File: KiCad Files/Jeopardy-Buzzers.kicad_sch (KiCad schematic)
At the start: 13 parts, among them J1 USB_C_Receptacle, U1 CH32V003FxUx, U2 CH340N, U3 NRF24L01_Breakout, U4 TPD2EUSB30, U5 AMS1117-3.3

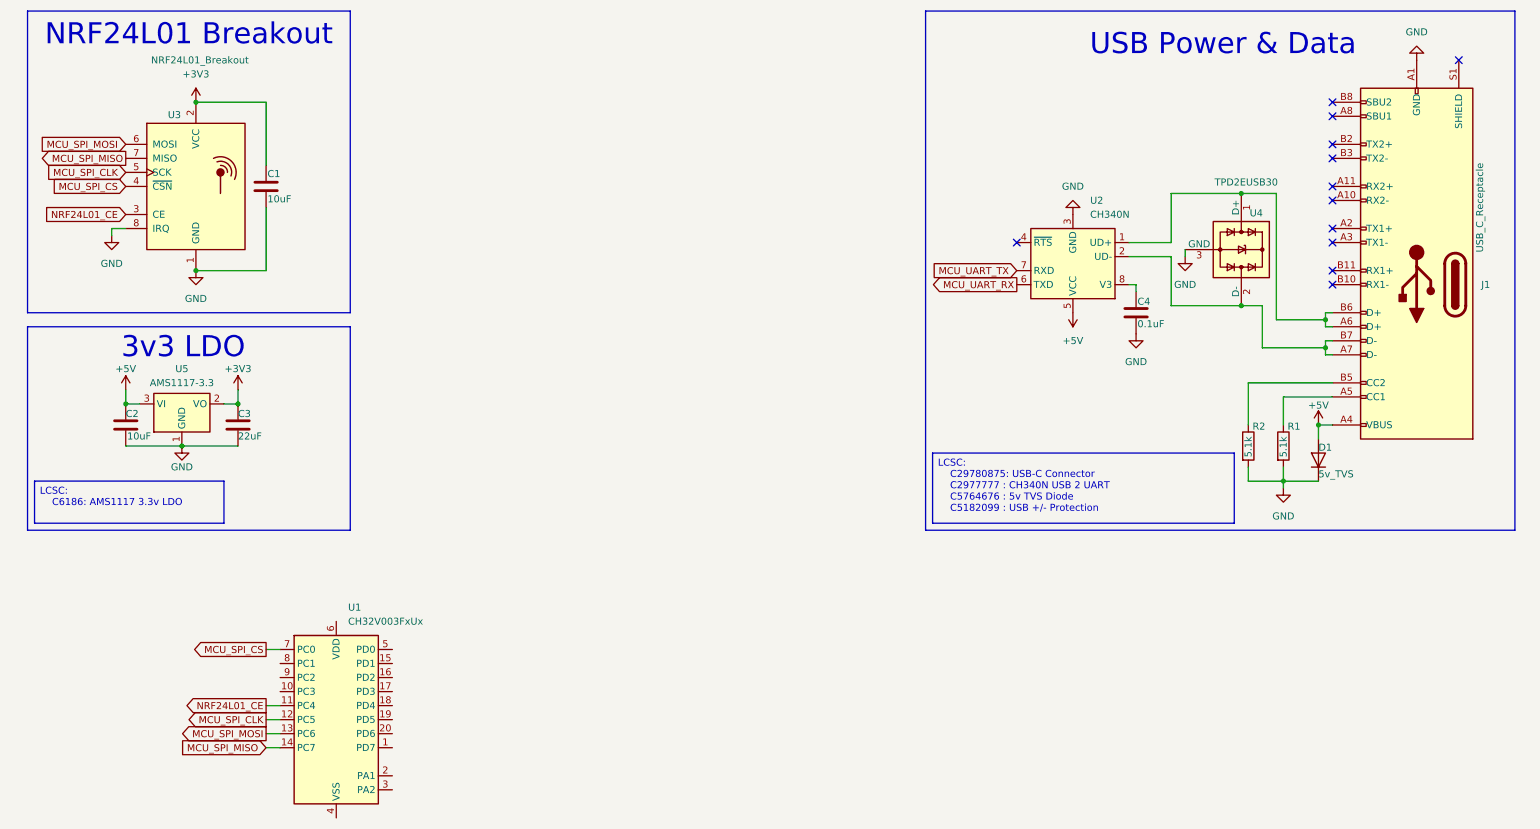
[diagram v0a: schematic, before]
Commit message: Added crystal and passives for MCU, also added Zener diodes for USB Protection. Connected UART to the CH340N USB2UART chip
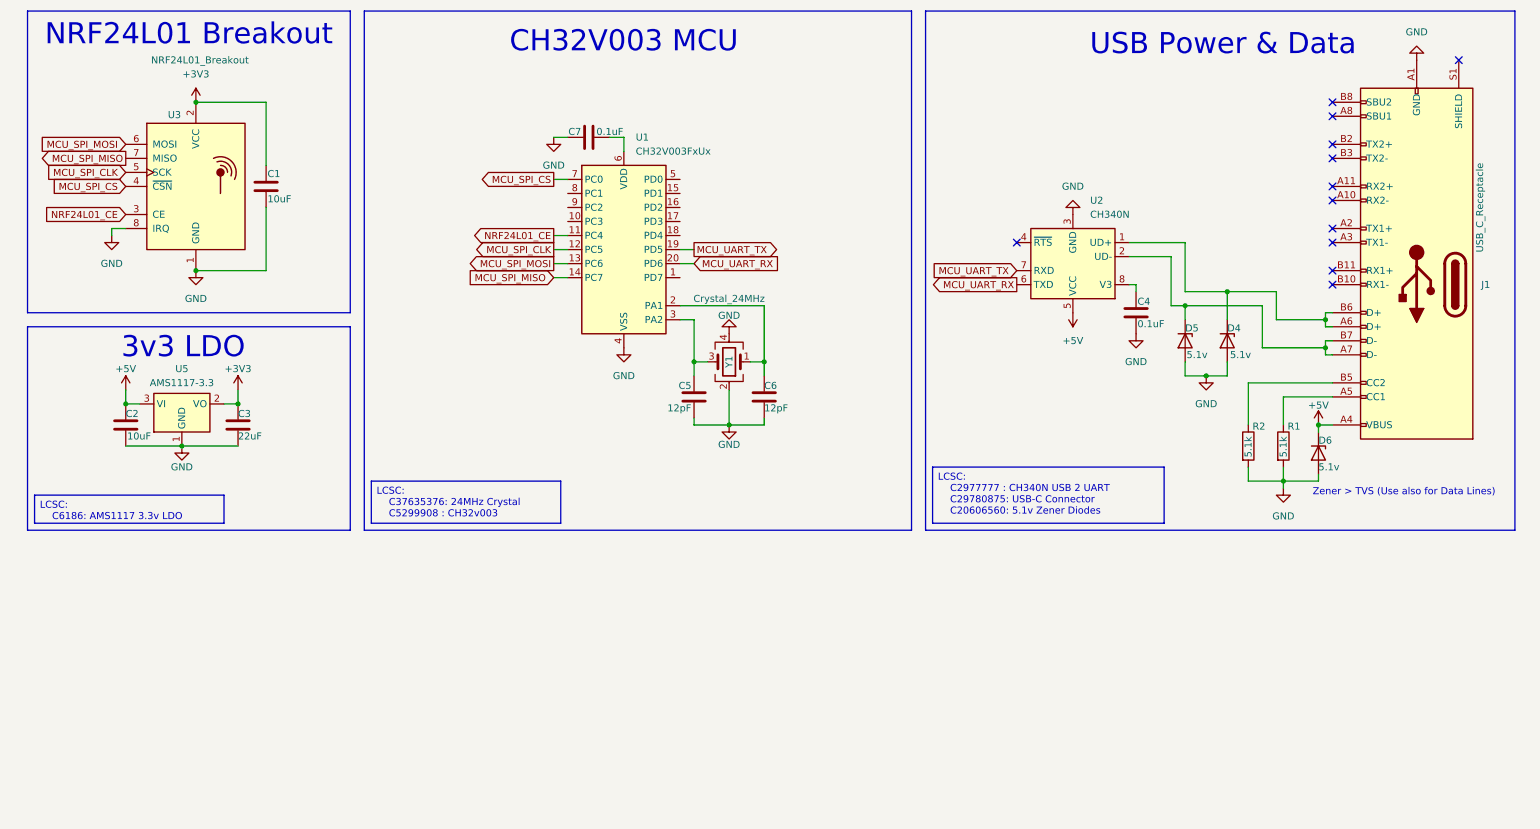
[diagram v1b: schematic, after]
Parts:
- removed D1: 5v_TVS, Diode_SMD:D_SMB, symbol Device:D
- removed U4: TPD2EUSB30, Package_TO_SOT_SMD:Texas_DRT-3, symbol Power_Protection:TPD2EUSB30
- added C5, C6: 12pF, Capacitor_SMD:C_0805_2012Metric, symbol Device:C
- added C7: 0.1uF, Capacitor_SMD:C_0805_2012Metric, symbol Device:C
- added D4, D5, D6: 5.1v, Diode_SMD:Nexperia_CFP3_SOD-123W, symbol Device:D_Zener
- added Y1: Crystal_24MHz, Crystal:Crystal_SMD_3225-4Pin_3.2x2.5mm, symbol Device:Crystal_GND24
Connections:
- net +5V: now also D6.1 (K)
- net GND: now also U1.21 (VSS), U1.4 (VSS), C5.2, C6.2, C7.1, D4.2 (A), D5.2 (A), D6.2 (A), Y1.2, Y1.4
- net MCU_UART_RX: now also U1.20 (PD6)
- net MCU_UART_TX: now also U1.19 (PD5)
- net at U1.2 (PA1): now also C6.1, Y1.1
- net at U1.3 (PA2): now also C5.1, Y1.3
- net at U1.6 (VDD): now also C7.2
- net at J1.A6 (D+), J1.B6 (D+), U2.1 (UD+): now also D4.1 (K)
- net at J1.A7 (D-), J1.B7 (D-), U2.2 (UD-): now also D5.1 (K)
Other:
- note added: "CH32V003 MCU"
- note added: "Zener > TVS (Use also for Data Lines)"
- moved on the sheet: U1

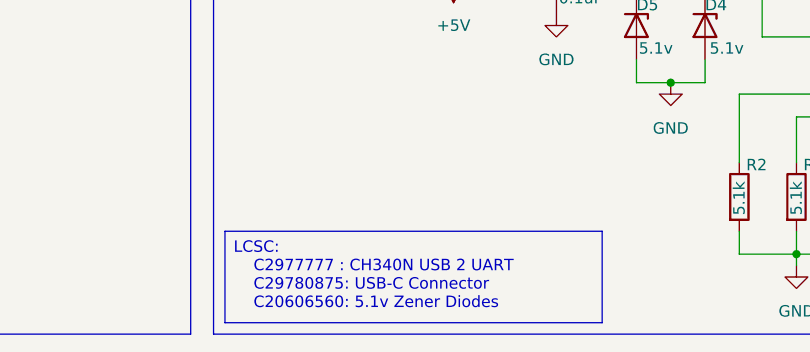
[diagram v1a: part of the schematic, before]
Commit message: Started Creating the USB-C connector footprint
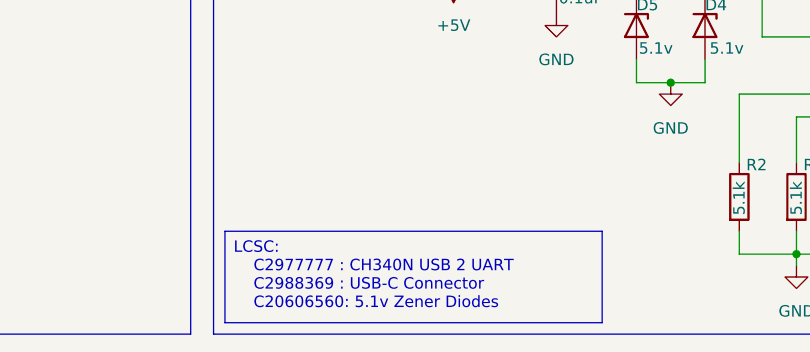
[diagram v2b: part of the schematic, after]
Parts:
- J1: footprint (none) -> Library:Usb-C
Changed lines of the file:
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@@
 		)
 	)
-	(text_box "LCSC:\n	C2977777 : CH340N USB 2 UART\n	C29780875: USB-C Connector\n	C20606560: 5.1v Zener Diodes"
+	(text_box "LCSC:\n	C2977777 : CH340N USB 2 UART\n	C2988369 : USB-C Connector\n	C20606560: 5.1v Zener Diodes"
 		(exclude_from_sim no)
 		(at 177.8 96.52 0)
@@
 			)
 		)
-		(property "Footprint" ""
+		(property "Footprint" "Library:Usb-C"
 			(at 261.62 63.5 0)
 			(effects

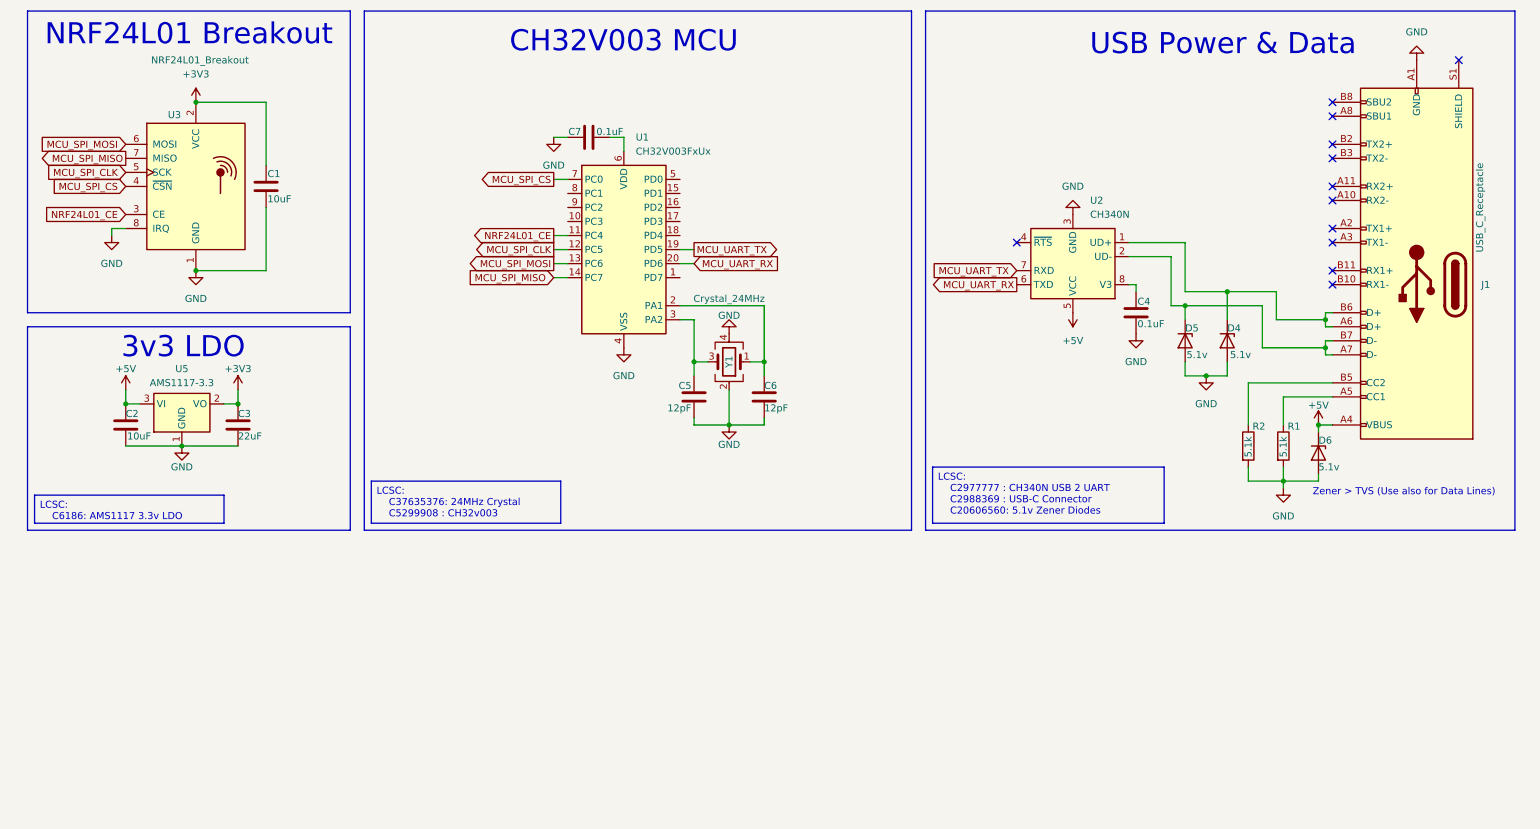
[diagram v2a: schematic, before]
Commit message: Changed footprints around, also added connectors
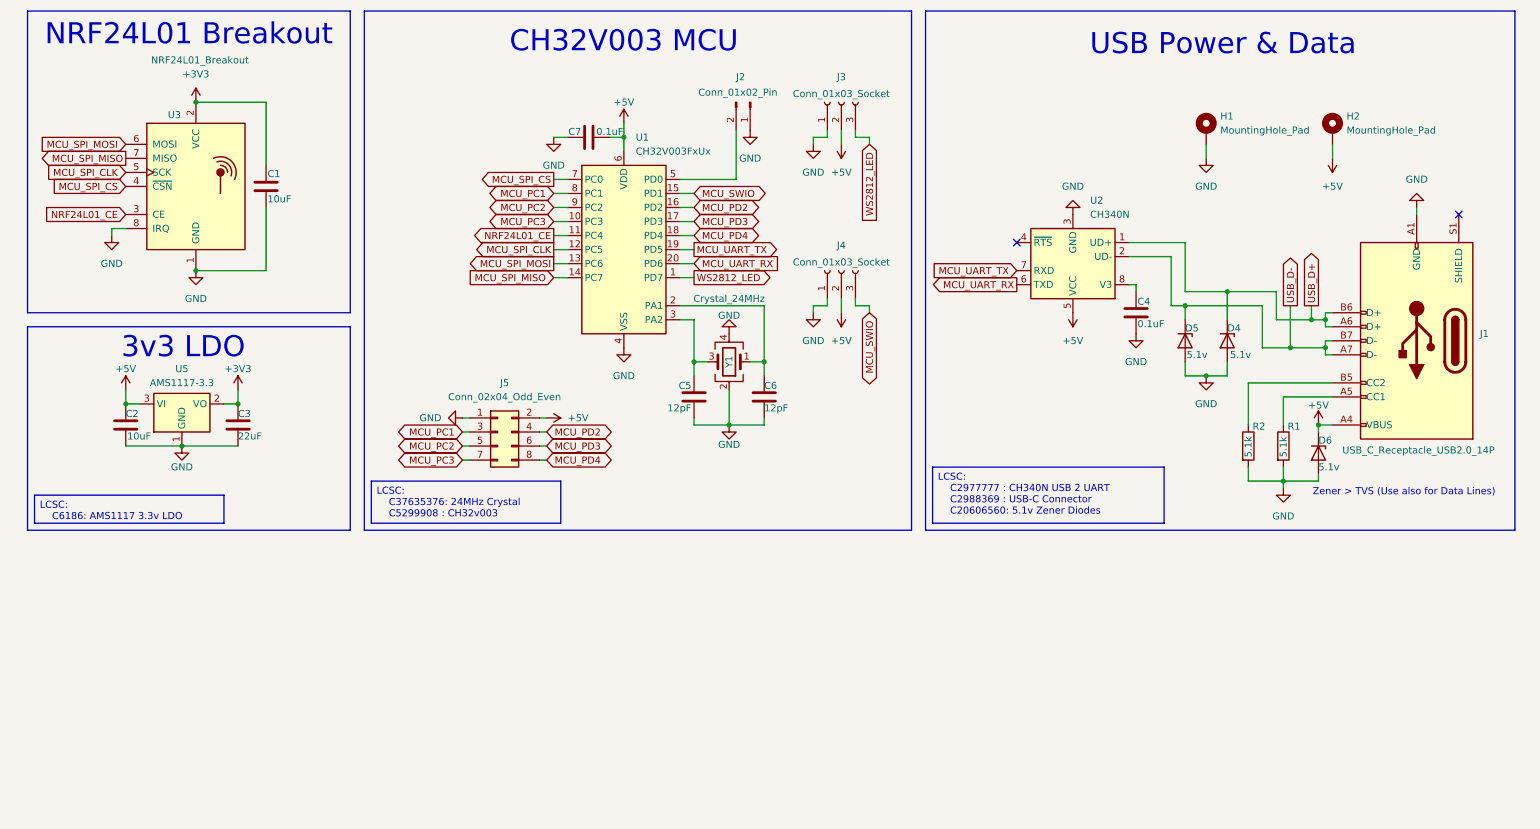
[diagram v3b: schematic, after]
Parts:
- removed J1: USB_C_Receptacle, Library:Usb-C, symbol Connector:USB_C_Receptacle
- added H1, H2: MountingHole_Pad, Connector_PinSocket_2.54mm:PinSocket_1x01_P2.54mm_Vertical, symbol Mechanical:MountingHole_Pad
- added J1: USB_C_Receptacle_USB2.0_14P, Library:Usb-C, symbol Connector:USB_C_Receptacle_USB2.0_14P
- added J2: Conn_01x02_Pin, Connector_PinHeader_2.54mm:PinHeader_1x02_P2.54mm_Vertical, symbol Connector:Conn_01x02_Pin
- added J3: Conn_01x03_Socket, Connector_JST:JST_PH_S3B-PH-K_1x03_P2.00mm_Horizontal, symbol Connector:Conn_01x03_Socket
- added J4: Conn_01x03_Socket, Connector_PinHeader_2.54mm:PinHeader_1x03_P2.54mm_Vertical, symbol Connector:Conn_01x03_Socket
- added J5: Conn_02x04_Odd_Even, Connector_PinHeader_2.54mm:PinHeader_2x04_P2.54mm_Vertical, symbol Connector_Generic:Conn_02x04_Odd_Even
- C1, C2, C3, C4: footprint Resistor_SMD:R_0805_2012Metric -> Capacitor_SMD:C_0603_1608Metric_Pad1.08x0.95mm_HandSolder
- C5, C6, C7: footprint Capacitor_SMD:C_0805_2012Metric -> Capacitor_SMD:C_0603_1608Metric_Pad1.08x0.95mm_HandSolder
- R1, R2: footprint Resistor_SMD:R_0805_2012Metric -> Resistor_SMD:R_0603_1608Metric_Pad0.98x0.95mm_HandSolder
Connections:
- net +5V: now also C7.2, U1.6 (VDD), H2.1, J1.A4 (VBUS), J1.A9 (VBUS), J1.B4 (VBUS), J1.B9 (VBUS), J3.2 (Pin_2), J4.2 (Pin_2), J5.2 (Pin_2)
- net GND: now also H1.1, J1.A1 (GND), J1.A12 (GND), J1.B1 (GND), J1.B12 (GND), J2.1 (Pin_1), J3.1 (Pin_1), J4.1 (Pin_1), J5.1 (Pin_1)
- net USB_D+: now reaches D4.1 (K), U2.1 (UD+)
- net USB_D+: now also J1.A6 (D+), J1.B6 (D+)
- net WS2812_LED: now reaches U1.1 (PD7)
- net WS2812_LED: now also J3.3 (Pin_3)
- net MCU_PC3: now reaches U1.10 (PC3)
- net MCU_PC3: now also J5.7 (Pin_7)
- net MCU_SWIO: now reaches U1.15 (PD1)
- net MCU_SWIO: now also J4.3 (Pin_3)
- net MCU_PD2: now reaches U1.16 (PD2)
- net MCU_PD2: now also J5.4 (Pin_4)
- net MCU_PD3: now reaches U1.17 (PD3)
- net MCU_PD3: now also J5.6 (Pin_6)
- net MCU_PD4: now reaches U1.18 (PD4)
- net MCU_PD4: now also J5.8 (Pin_8)
- net at U1.5 (PD0): now also J2.2 (Pin_2)
- net MCU_PC1: now reaches U1.8 (PC1)
- net MCU_PC1: now also J5.3 (Pin_3)
- net MCU_PC2: now reaches U1.9 (PC2)
- net MCU_PC2: now also J5.5 (Pin_5)
- net USB_D-: now reaches D5.1 (K), U2.2 (UD-)
- net USB_D-: now also J1.A7 (D-), J1.B7 (D-)
- net at R1.1: now also J1.A5 (CC1)
- net at R2.1: now also J1.B5 (CC2)
- no-connect marks 12 -> 2
